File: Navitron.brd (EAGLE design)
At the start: 70 x 70 mm, 78 parts, among them J2 DX07S016JA1R1500, Q1 ROHM_RUM002N02T2LROHM_RUM002N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, Q2 2.5A/30V, Q3 ROHM_RUM002N02T2LROHM_RUM002N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, Q4 ROHM_RUM002N02T2LROHM_RUM002N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, Q5 ROHM_RUM002N02T2LROHM_RUM002N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, T1 BC847, T2 BC847, U1 ESP32-WROOM-32, U2 9DoF IMU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

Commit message: Pad Renaming
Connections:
- net N$12 renamed LED1.8_2
- net N$13 renamed LED1.8
- net N$14 renamed SDA_W_2
- net N$15 renamed SDA_W_1
- new net !CS: U2.22
- new net !CTS: U5.9
- new net !DCD: U5.12
- new net !DSR: U5.10
- new net !RI: U5.11
- new net AD0/SD0: U2.9
- new net AUX_CL: U2.7
- new net AUX_DA: U2.21
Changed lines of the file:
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@@
 <wire x1="21.742" y1="49" x2="19.477" y2="49" width="0.3048" layer="1"/>
 </signal>
-<signal name="N$12">
+<signal name="LED1.8_2">
 <contactref element="R12" pad="2"/>
 <contactref element="POWER2" pad="C"/>
@@
 <wire x1="50.14" y1="53.487" x2="50.14" y2="53.54" width="0.3048" layer="1"/>
 </signal>
-<signal name="N$13">
+<signal name="LED1.8">
 <contactref element="POWER2" pad="A"/>
 <contactref element="JP3" pad="2"/>
@@
 <wire x1="63.20841875" y1="20.526365625" x2="59.1667875" y2="13.095953125" width="0.3048" layer="1"/>
 </signal>
-<signal name="N$14">
+<signal name="SDA_W_2">
 <contactref element="JP5" pad="3"/>
 <contactref element="R16" pad="2"/>
@@
 <wire x1="57.44075" y1="29.15" x2="57.80675" y2="29.516" width="0.3048" layer="1"/>
 </signal>
-<signal name="N$15">
+<signal name="SDA_W_1">
 <contactref element="JP5" pad="1"/>
 <contactref element="R14" pad="2"/>
@@
 <wire x1="50.85815" y1="48" x2="51.85815" y2="47" width="0.1524" layer="16"/>
 </signal>
+<signal name="AUX_CL">
+<contactref element="U2" pad="7"/>
+</signal>
+<signal name="AUX_DA">
+<contactref element="U2" pad="21"/>
+</signal>
+<signal name="!CS">
+<contactref element="U2" pad="22"/>
+</signal>
+<signal name="AD0/SD0">
+<contactref element="U2" pad="9"/>
+</signal>
+<signal name="!DCD">
+<contactref element="U5" pad="12"/>
+</signal>
+<signal name="!RI">
+<contactref element="U5" pad="11"/>
+</signal>
+<signal name="!DSR">
+<contactref element="U5" pad="10"/>
+</signal>
+<signal name="!CTS">
+<contactref element="U5" pad="9"/>
+</signal>
 </signals>

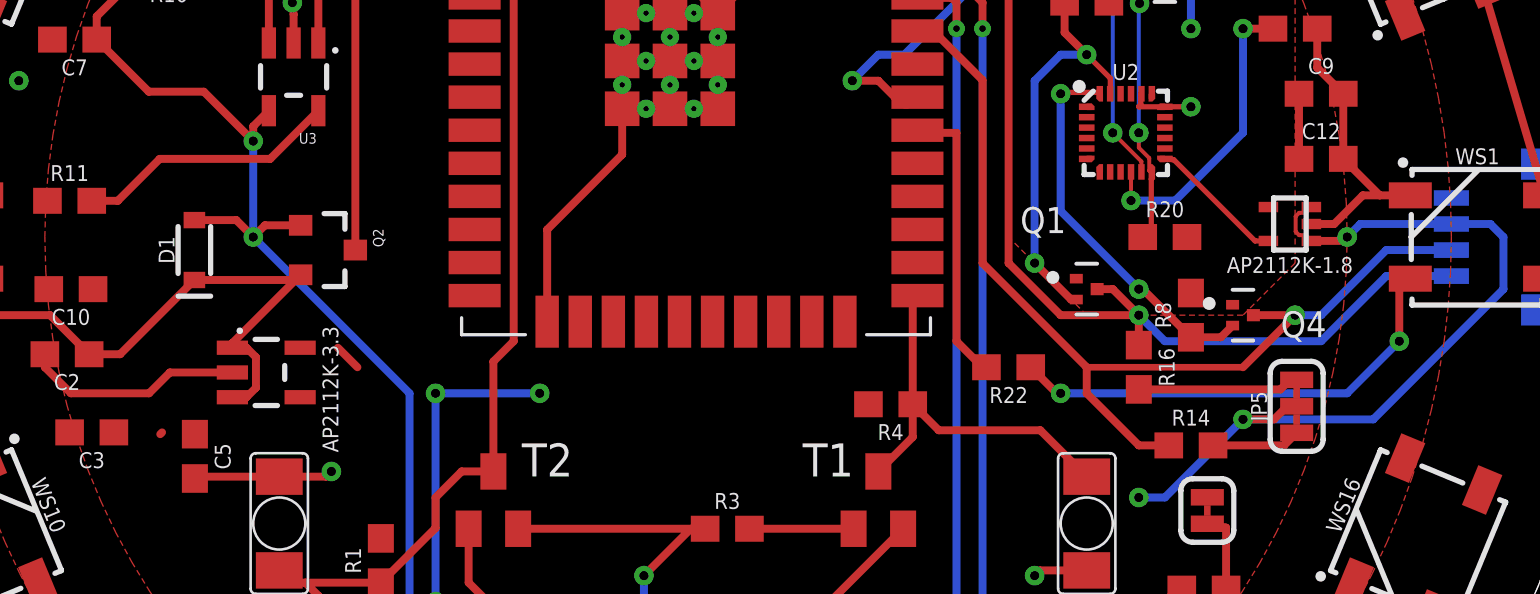
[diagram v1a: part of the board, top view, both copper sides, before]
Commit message: Change Voltage Regulator and Resistor Value
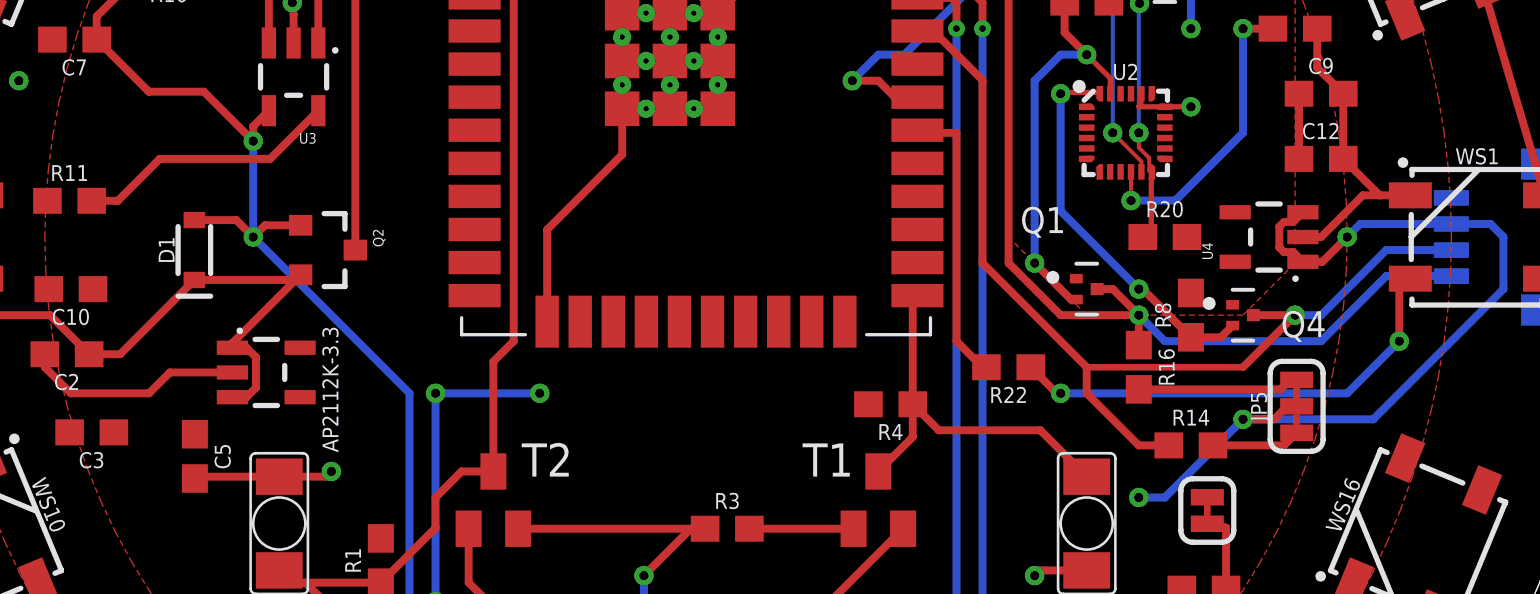
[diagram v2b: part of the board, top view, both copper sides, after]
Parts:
- removed AP2112K-1.8: 1.8V/100mA, SparkFun-IC-Power:SC70
- added U4: AP2112K-1.8V, SparkFun-IC-Power-Customized:SOT23-5
- R12: value 1k -> 560
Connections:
- net 1.8V: now also U4.5; no longer AP2112K-1.8.5
- net 3.3V: now also U4.1, U4.3; no longer AP2112K-1.8.1, AP2112K-1.8.3
- net GND: now also U4.2; no longer AP2112K-1.8.2
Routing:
- net 1.8V: track 18.6 -> 13.5 mm
- net 3.3V: track 52.4 -> 53.0 mm
- net GND: track 78.3 -> 78.8 mm

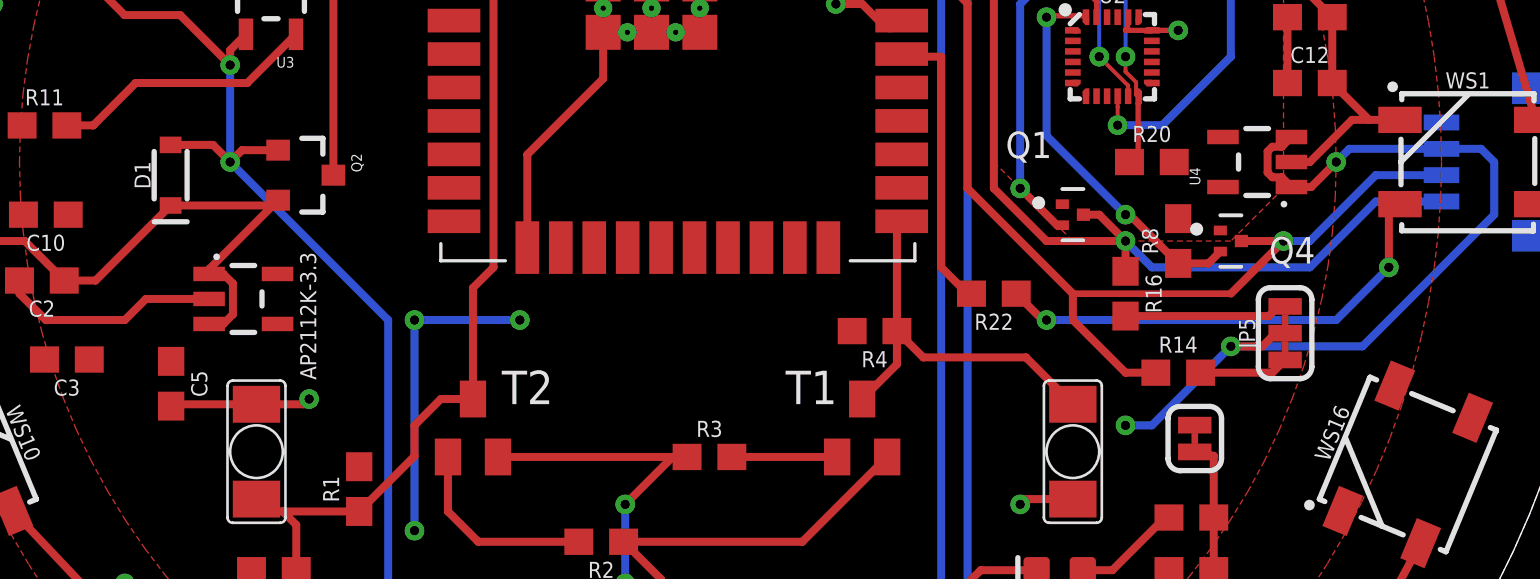
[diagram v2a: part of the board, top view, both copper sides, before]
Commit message: Change C5 Position
- Moved Capacitor closer to the 1.8V Voltage Regulator.
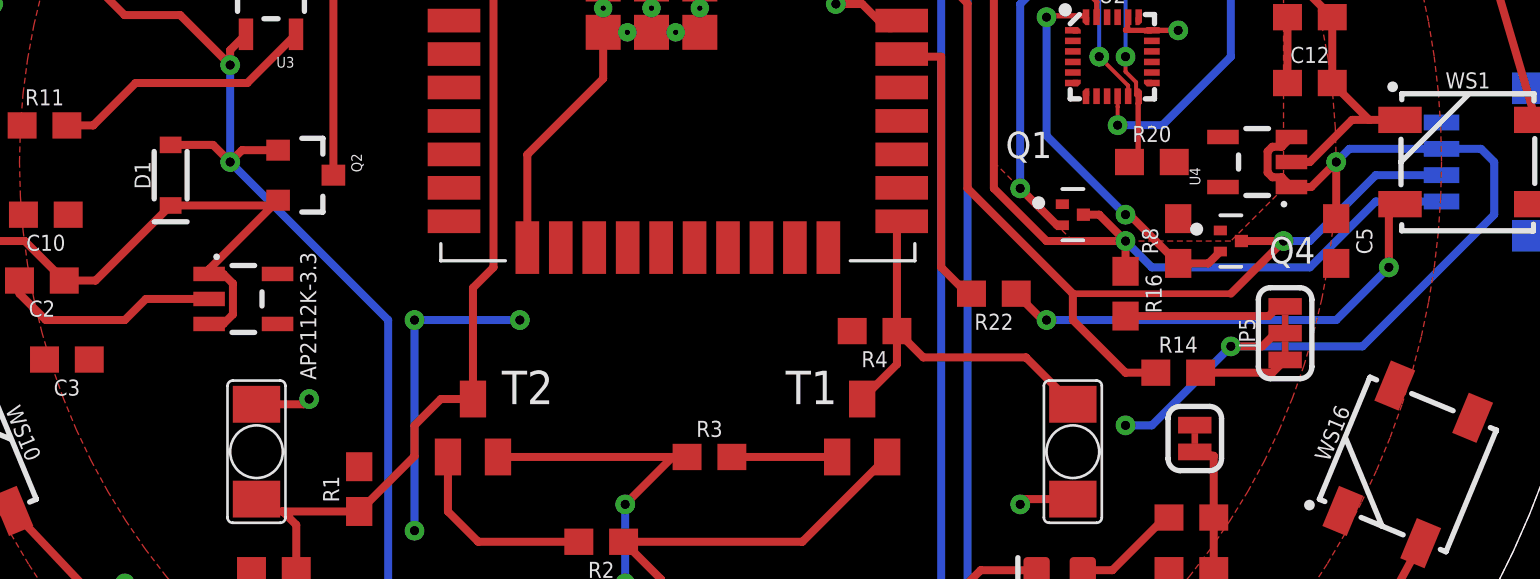
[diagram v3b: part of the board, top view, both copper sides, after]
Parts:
- moved C5 44.6 mm to (60.0, 32.0)
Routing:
- net GND: track 78.8 -> 75.9 mm
- net 3.3V: track 53.0 -> 55.2 mm
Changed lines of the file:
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@@
 <attribute name="VALUE" x="47.23" y="12.738" size="0.6096" layer="27" font="vector" ratio="20" align="top-center"/>
 </element>
-<element name="C5" library="SparkFun-Capacitors" package="0603" value="1.0uF" x="15.76" y="26.58" smashed="yes" rot="R270">
-<attribute name="NAME" x="16.522" y="26.58" size="0.6096" layer="25" font="vector" ratio="20" rot="R270" align="bottom-center"/>
-<attribute name="PROD_ID" value="CAP-00810" x="-52.82" y="11.34" size="1.778" layer="27" rot="R270" display="off"/>
-<attribute name="VALUE" x="14.998" y="26.58" size="0.6096" layer="27" font="vector" ratio="20" rot="R270" align="top-center"/>
+<element name="C5" library="SparkFun-Capacitors" package="0603" value="1.0uF" x="60" y="32" smashed="yes" rot="R270">
+<attribute name="NAME" x="60.762" y="32" size="0.6096" layer="25" font="vector" ratio="20" rot="R270" align="bottom-center"/>
+<attribute name="PROD_ID" value="CAP-00810" x="-8.58" y="16.76" size="1.778" layer="27" rot="R270" display="off"/>
+<attribute name="VALUE" x="59.238" y="32" size="0.6096" layer="27" font="vector" ratio="20" rot="R270" align="top-center"/>
 </element>
 <element name="C7" library="SparkFun-Capacitors" package="0603" value="1.0uF" x="11.14" y="42.58" smashed="yes" rot="R180">
@@
 <contactref element="U$1" pad="P$1"/>
 <contactref element="U$2" pad="P$1"/>
-<wire x1="19" y1="25.8" x2="15.83" y2="25.8" width="0.3048" layer="1"/>
-<wire x1="15.83" y1="25.8" x2="15.76" y2="25.73" width="0.3048" layer="1"/>
+<wire x1="59.83" y1="30.8" x2="60" y2="31.15" width="0.3048" layer="1"/>
 <wire x1="19" y1="25.8" x2="20.8" y2="25.8" width="0.3048" layer="1"/>
 <wire x1="20.8" y1="25.8" x2="21" y2="26" width="0.3048" layer="1"/>
@@
 <wire x1="59" y1="35" x2="58.3001" y2="35" width="0.3048" layer="1"/>
 <wire x1="60.6" y1="36.6" x2="59" y2="35" width="0.3048" layer="1"/>
+<wire x1="58.85" y1="43" x2="62.224353125" y2="43.487371875" width="0" layer="19" extent="1-1"/>
+<wire x1="64" y1="36.5" x2="62.423" y2="36.6" width="0" layer="19" extent="1-16"/>
+<wire x1="60" y1="31.15" x2="58.3001" y2="35" width="0" layer="19" extent="1-1"/>
+<wire x1="54" y1="40" x2="58.85" y2="43" width="0" layer="19" extent="1-1"/>
+<wire x1="58" y1="49" x2="58.85" y2="43" width="0" layer="19" extent="1-1"/>
+<wire x1="53.259615625" y1="55.522359375" x2="58" y2="49" width="0" layer="19" extent="1-1"/>
+<wire x1="50.14" y1="55.24" x2="53.259615625" y2="55.522359375" width="0" layer="19" extent="1-1"/>
+<wire x1="50" y1="57" x2="50.14" y2="55.24" width="0" layer="19" extent="1-1"/>
+<wire x1="48.249046875" y1="60.252003125" x2="50" y2="57" width="0" layer="19" extent="1-1"/>
+<wire x1="43.5" y1="49.26" x2="50.14" y2="55.24" width="0" layer="19" extent="1-1"/>
+<wire x1="34.9175" y1="43.595" x2="35.835" y2="43.595" width="0" layer="19" extent="1-1"/>
+<wire x1="34" y1="43.595" x2="34.9175" y2="43.595" width="0" layer="19" extent="1-1"/>
+<wire x1="33.0825" y1="43.595" x2="34" y2="43.595" width="0" layer="19" extent="1-1"/>
+<wire x1="35.835" y1="42.6775" x2="35.835" y2="43.595" width="0" layer="19" extent="1-1"/>
+<wire x1="35.835" y1="41.76" x2="35.835" y2="42.6775" width="0" layer="19" extent="1-1"/>
+<wire x1="35.835" y1="40.8425" x2="35.835" y2="41.76" width="0" layer="19" extent="1-1"/>
+<wire x1="32.165" y1="43.595" x2="33.0825" y2="43.595" width="0" layer="19" extent="1-1"/>
+<wire x1="35.835" y1="39.925" x2="35.835" y2="40.8425" width="0" layer="19" extent="1-1"/>
 <wire x1="34" y1="42.6775" x2="34" y2="43.595" width="0" layer="19" extent="1-1"/>
-<wire x1="35.835" y1="41.76" x2="34.9175" y2="41.76" width="0" layer="19" extent="1-1"/>
-<wire x1="32.165" y1="43.595" x2="32.165" y2="42.6775" width="0" layer="19" extent="1-1"/>
-<wire x1="34" y1="41.76" x2="34" y2="40.8425" width="0" layer="19" extent="1-1"/>
-<wire x1="35.835" y1="39.925" x2="34.9175" y2="39.925" width="0" layer="19" extent="1-1"/>
-<wire x1="35.835" y1="43.595" x2="35.835" y2="42.6775" width="0" layer="19" extent="1-1"/>
-<wire x1="32.165" y1="41.76" x2="32.165" y2="40.8425" width="0" layer="19" extent="1-1"/>
-<wire x1="34" y1="39.925" x2="34.9175" y2="39.925" width="0" layer="19" extent="1-1"/>
-<wire x1="32.165" y1="39.925" x2="33.0825" y2="39.925" width="0" layer="19" extent="1-1"/>
+<wire x1="34" y1="41.76" x2="34" y2="42.6775" width="0" layer="19" extent="1-1"/>
+<wire x1="33.0825" y1="41.76" x2="34" y2="41.76" width="0" layer="19" extent="1-1"/>
+<wire x1="34.9175" y1="41.76" x2="35.835" y2="41.76" width="0" layer="19" extent="1-1"/>
+<wire x1="34" y1="40.8425" x2="34" y2="41.76" width="0" layer="19" extent="1-1"/>
+<wire x1="32.165" y1="41.76" x2="33.0825" y2="41.76" width="0" layer="19" extent="1-1"/>
+<wire x1="34" y1="39.925" x2="34" y2="40.8425" width="0" layer="19" extent="1-1"/>
+<wire x1="32.165" y1="42.6775" x2="32.165" y2="43.595" width="0" layer="19" extent="1-1"/>
+<wire x1="32.165" y1="40.8425" x2="32.165" y2="41.76" width="0" layer="19" extent="1-1"/>
+<wire x1="33.0825" y1="39.925" x2="34" y2="39.925" width="0" layer="19" extent="1-1"/>
+<wire x1="34.9175" y1="39.925" x2="35.835" y2="39.925" width="0" layer="19" extent="1-1"/>
+<wire x1="32.165" y1="39.925" x2="32.165" y2="40.8425" width="0" layer="19" extent="1-1"/>
+<wire x1="19.5" y1="44" x2="26.5" y2="49.26" width="0" layer="19" extent="1-1"/>
+<wire x1="13.81" y1="49" x2="19.5" y2="44" width="0" layer="19" extent="1-1"/>
+<wire x1="12" y1="50" x2="13.81" y2="49" width="0" layer="19" extent="1-1"/>
+<wire x1="9.74799375" y1="48.249046875" x2="12" y2="50" width="0" layer="19" extent="1-1"/>
+<wire x1="14.4776375" y1="53.259615625" x2="12" y2="50" width="0" layer="19" extent="1-1"/>
+<wire x1="10.29" y1="42.58" x2="9.74799375" y2="48.249046875" width="0" layer="19" extent="1-1"/>
+<wire x1="9" y1="41" x2="10.29" y2="42.58" width="0" layer="19" extent="1-1"/>
+<wire x1="10.1" y1="36.39" x2="9" y2="41" width="0" layer="19" extent="1-1"/>
+<wire x1="10.15" y1="33" x2="10.1" y2="36.39" width="0" layer="19" extent="1-1"/>
+<wire x1="10" y1="30.5" x2="10.15" y2="33" width="0" layer="19" extent="1-1"/>
+<wire x1="7.577" y1="33.4" x2="10.15" y2="33" width="0" layer="19" extent="1-1"/>
+<wire x1="10.95" y1="27.5" x2="10" y2="30.5" width="0" layer="19" extent="1-1"/>
+<wire x1="7.77564375" y1="26.512625" x2="10.95" y2="27.5" width="0" layer="19" extent="1-1"/>
+<wire x1="19" y1="25.8" x2="17.1999" y2="29.8" width="0" layer="19" extent="1-1"/>
+<wire x1="18.81" y1="19.5" x2="19" y2="25.8" width="0" layer="19" extent="1-1"/>
+<wire x1="14" y1="19" x2="18.81" y2="19.5" width="0" layer="19" extent="1-1"/>
+<wire x1="21.75095" y1="9.74799375" x2="16.74038125" y2="14.4776375" width="0" layer="19" extent="1-1"/>
+<wire x1="30" y1="10" x2="21.75095" y2="9.74799375" width="0" layer="19" extent="1-1"/>
+<wire x1="32" y1="13.35" x2="30.555" y2="12" width="0" layer="19" extent="1-16"/>
+<wire x1="31.9" y1="6.7" x2="30" y2="10" width="0" layer="19" extent="1-16"/>
+<wire x1="34.5" y1="9" x2="31.9" y2="6.7" width="0" layer="19" extent="16-16"/>
+<wire x1="36.6" y1="7.577" x2="34.5" y2="9" width="0" layer="19" extent="1-1"/>
+<wire x1="38.1" y1="6.7" x2="36.6" y2="7.577" width="0" layer="19" extent="1-16"/>
+<wire x1="40" y1="9" x2="38.1" y2="6.7" width="0" layer="19" extent="16-16"/>
+<wire x1="43.487371875" y1="7.77564375" x2="40" y2="9" width="0" layer="19" extent="1-1"/>
+<wire x1="48.08" y1="13.5" x2="43.487371875" y2="7.77564375" width="0" layer="19" extent="1-1"/>
+<wire x1="55.522359375" y1="16.74038125" x2="48.08" y2="13.5" width="0" layer="19" extent="1-1"/>
+<wire x1="60.252003125" y1="21.75095" x2="55.522359375" y2="16.74038125" width="0" layer="19" extent="1-1"/>
+<wire x1="50" y1="22.2" x2="55.522359375" y2="16.74038125" width="0" layer="19" extent="1-1"/>
+<wire x1="28.48" y1="59.58" x2="26.5" y2="49.26" width="0" layer="19" extent="1-1"/>
+<wire x1="26.512625" y1="62.224353125" x2="28.48" y2="59.58" width="0" layer="19" extent="1-1"/>
+<wire x1="33.4" y1="62.423" x2="28.48" y2="59.58" width="0" layer="19" extent="1-1"/>
+<wire x1="36" y1="61.7" x2="33.4" y2="62.423" width="0" layer="19" extent="1-16"/>
 </signal>
 <signal name="3.3V">
@@
 <wire x1="57.57385" y1="34.4202" x2="57.9299" y2="34.4202" width="0.3048" layer="1"/>
 <wire x1="57.9299" y1="34.4202" x2="58.3001" y2="34.05" width="0.3048" layer="1"/>
+<wire x1="60" y1="32.85" x2="60" y2="35" width="0.3048" layer="1"/>
 <wire x1="47.85" y1="52" x2="54" y2="51" width="0" layer="19" extent="1-1"/>
 <wire x1="58.3001" y1="35.95" x2="56.85" y2="45" width="0" layer="19" extent="1-1"/>
@@
 <wire x1="22.9" y1="23.43" x2="25" y2="21" width="0" layer="19" extent="1-1"/>
 <wire x1="19.8001" y1="30.75" x2="25" y2="29" width="0" layer="19" extent="1-1"/>
-<wire x1="15.76" y1="27.43" x2="19.8001" y2="30.75" width="0" layer="19" extent="1-1"/>
-<wire x1="12.65" y1="27.5" x2="15.76" y2="27.43" width="0" layer="19" extent="1-1"/>
+<wire x1="30.555" y1="17.6" x2="25" y2="21" width="0" layer="19" extent="1-1"/>
+<wire x1="12.65" y1="27.5" x2="19.8001" y2="30.75" width="0" layer="19" extent="1-1"/>
 <wire x1="11.85" y1="33" x2="12.65" y2="27.5" width="0" layer="19" extent="1-1"/>
-<wire x1="30.555" y1="17.6" x2="25" y2="21" width="0" layer="19" extent="1-1"/>
 <wire x1="26.5" y1="47.99" x2="19.8001" y2="30.75" width="0" layer="19" extent="1-1"/>
 <wire x1="22.758" y1="49" x2="26.5" y2="47.99" width="0" layer="19" extent="1-1"/>
